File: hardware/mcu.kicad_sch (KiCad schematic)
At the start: 9 parts, among them J2 DebugEdge_02x03, SW1 RESET, U1 STM32G070CBTx_u, X1 KC2520Z

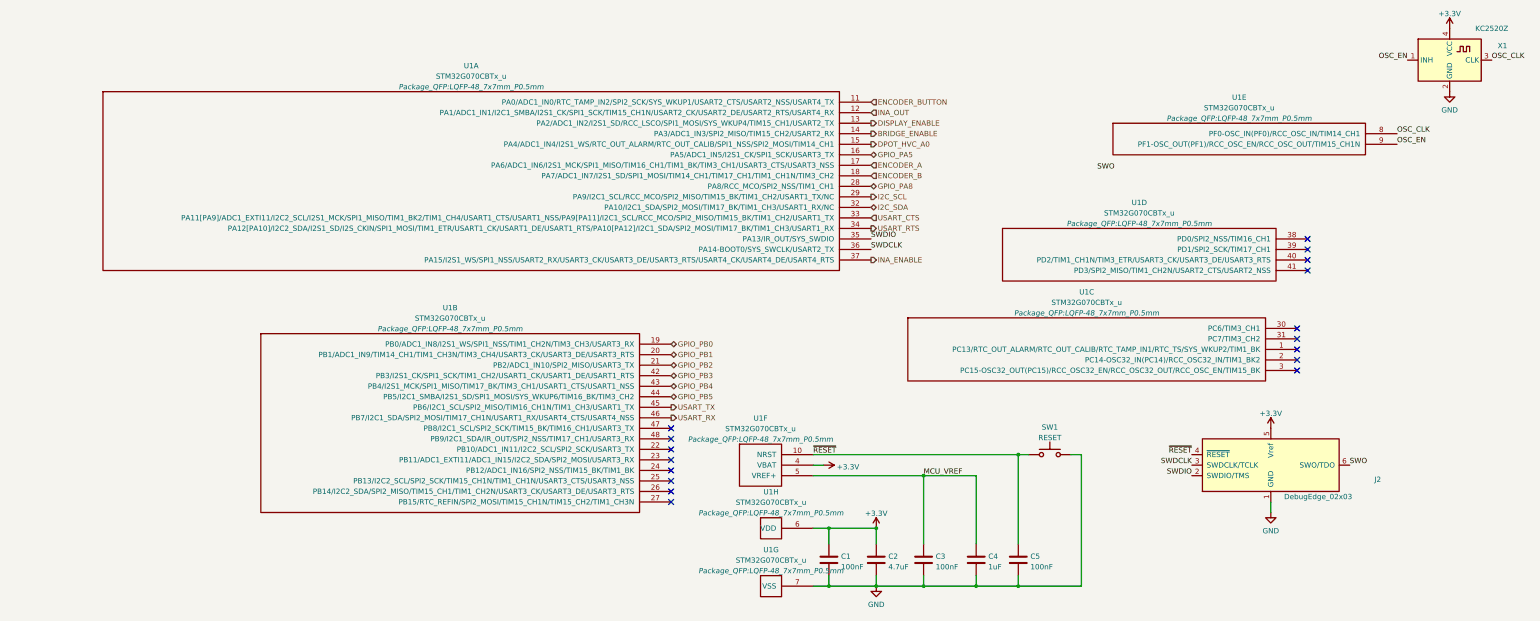
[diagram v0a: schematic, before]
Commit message: Updated schematic according to reference design
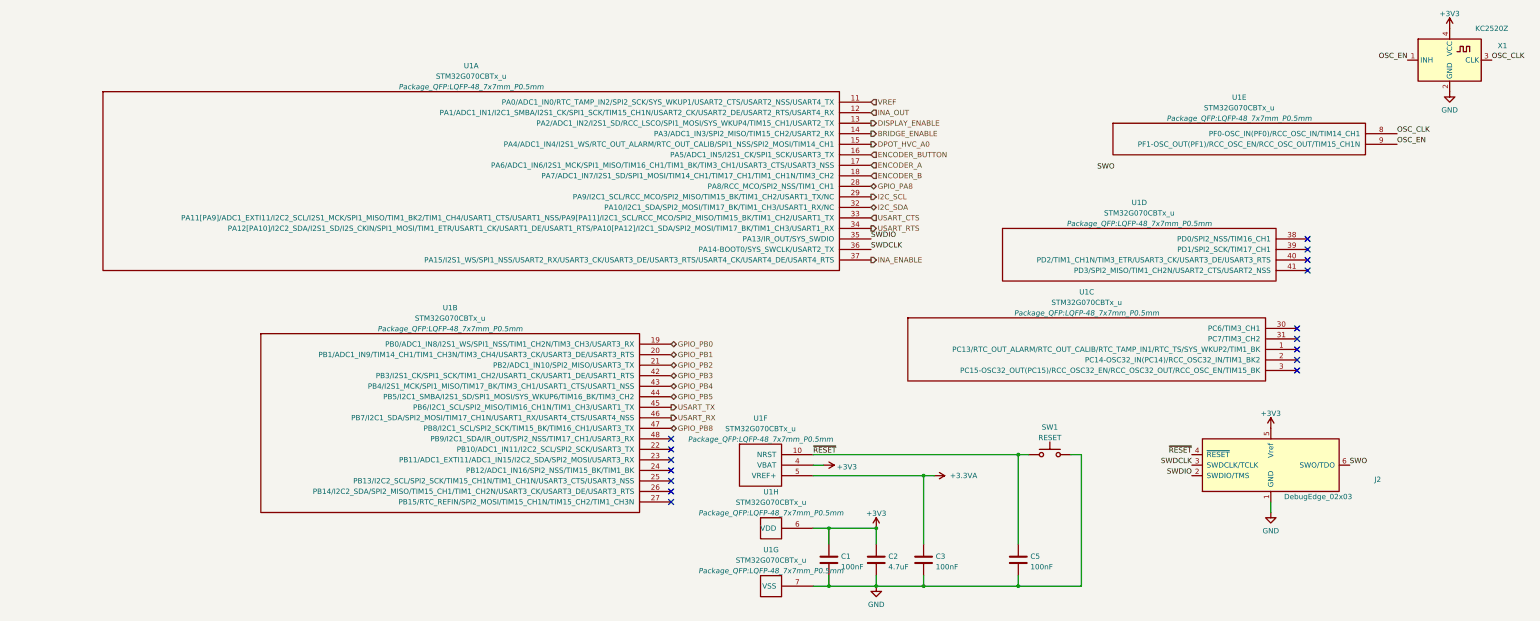
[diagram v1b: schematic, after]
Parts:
- removed C4: 1uF, Capacitor_SMD:C_0603_1608Metric_Pad1.08x0.95mm_HandSolder, symbol Device:C
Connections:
- net GPIO_PA5 is gone; now on net ENCODER_BUTTON: U1.16 (PA5/ADC1_IN5/I2S1_CK/SPI1_SCK/USART3_TX)
- net ENCODER_BUTTON: no longer U1.11 (PA0/ADC1_IN0/RTC_TAMP_IN2/SPI2_SCK/SYS_WKUP1/USART2_CTS/USART2_NSS/USART4_TX)
- net GPIO_PB8: now reaches U1.47 (PB8/I2C1_SCL/SPI2_SCK/TIM15_BK/TIM16_CH1/USART3_TX)
- net MCU_VREF renamed +3.3VA
- new net VREF: U1.11 (PA0/ADC1_IN0/RTC_TAMP_IN2/SPI2_SCK/SYS_WKUP1/USART2_CTS/USART2_NSS/USART4_TX)
- no-connect marks 17 -> 16

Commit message: Include active filter, ext. ADC, changes to power supply
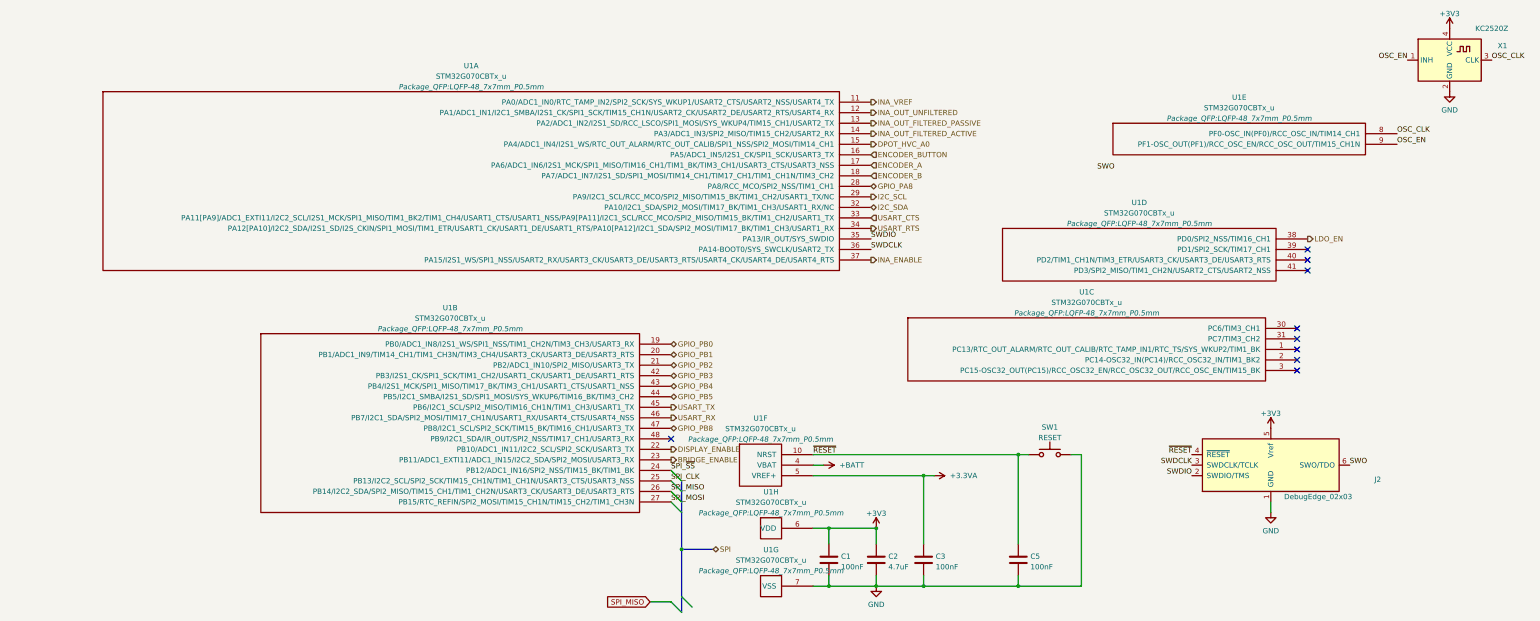
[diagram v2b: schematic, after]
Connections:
- net +3V3: no longer U1.4 (VBAT)
- net BRIDGE_ENABLE: now also U1.23 (PB11/ADC1_EXTI11/ADC1_IN15/I2C2_SDA/SPI2_MOSI/USART3_RX); no longer U1.14 (PA3/ADC1_IN3/SPI2_MISO/TIM15_CH2/USART2_RX)
- net DISPLAY_ENABLE: now also U1.22 (PB10/ADC1_IN11/I2C2_SCL/SPI2_SCK/USART3_TX); no longer U1.13 (PA2/ADC1_IN2/I2S1_SD/RCC_LSCO/SPI1_MOSI/SYS_WKUP4/TIM15_CH1/USART2_TX)
- net LDO_EN: now reaches U1.38 (PD0/SPI2_NSS/TIM16_CH1)
- net SPI_~{SS}: now reaches U1.24 (PB12/ADC1_IN16/SPI2_NSS/TIM15_BK/TIM1_BK)
- net SPI_CLK: now reaches U1.25 (PB13/I2C2_SCL/SPI2_SCK/TIM15_CH1N/TIM1_CH1N/USART3_CTS/USART3_NSS)
- net SPI_MISO: now reaches U1.26 (PB14/I2C2_SDA/SPI2_MISO/TIM15_CH1/TIM1_CH2N/USART3_CK/USART3_DE/USART3_RTS)
- net SPI_MOSI: now reaches U1.27 (PB15/RTC_REFIN/SPI2_MOSI/TIM15_CH1N/TIM15_CH2/TIM1_CH3N)
- net INA_OUT renamed INA_OUT_UNFILTERED
- net VREF renamed INA_VREF
- new net +BATT: U1.4 (VBAT)
- new net INA_OUT_FILTERED_ACTIVE: U1.14 (PA3/ADC1_IN3/SPI2_MISO/TIM15_CH2/USART2_RX)
- new net INA_OUT_FILTERED_PASSIVE: U1.13 (PA2/ADC1_IN2/I2S1_SD/RCC_LSCO/SPI1_MOSI/SYS_WKUP4/TIM15_CH1/USART2_TX)
- no-connect marks 16 -> 9

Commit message: Added correct symbol and libraries for ADC
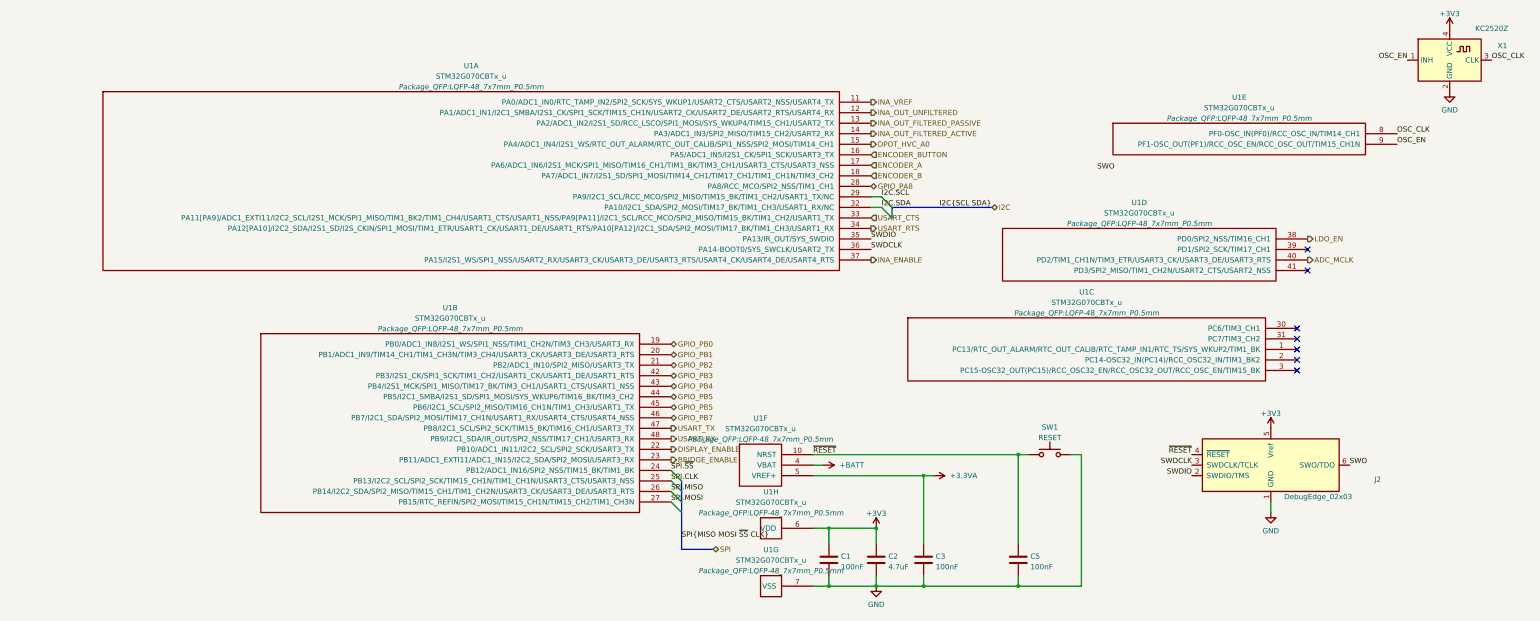
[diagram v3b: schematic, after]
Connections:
- net GPIO_PB8 is gone; now on net USART_TX: U1.47 (PB8/I2C1_SCL/SPI2_SCK/TIM15_BK/TIM16_CH1/USART3_TX)
- net GPIO_PB5: now also U1.45 (PB6/I2C1_SCL/SPI2_MISO/TIM16_CH1N/TIM1_CH3/USART1_TX)
- net USART_RX: now also U1.48 (PB9/I2C1_SDA/IR_OUT/SPI2_NSS/TIM17_CH1/USART3_RX); no longer U1.46 (PB7/I2C1_SDA/SPI2_MOSI/TIM17_CH1N/USART1_RX/USART4_CTS/USART4_NSS)
- net USART_TX: no longer U1.45 (PB6/I2C1_SCL/SPI2_MISO/TIM16_CH1N/TIM1_CH3/USART1_TX)
- net ADC_MCLK: now reaches U1.40 (PD2/TIM1_CH1N/TIM3_ETR/USART3_CK/USART3_DE/USART3_RTS)
- net I2C_SCL renamed I2C.SCL
- net I2C_SDA renamed I2C.SDA
- net SPI_CLK renamed SPI.CLK
- net SPI_MISO renamed SPI.MISO
- net SPI_MOSI renamed SPI.MOSI
- net SPI_~{SS} renamed SPI.~{SS}
- new net GPIO_PB7: U1.46 (PB7/I2C1_SDA/SPI2_MOSI/TIM17_CH1N/USART1_RX/USART4_CTS/USART4_NSS)
- no-connect marks 9 -> 7

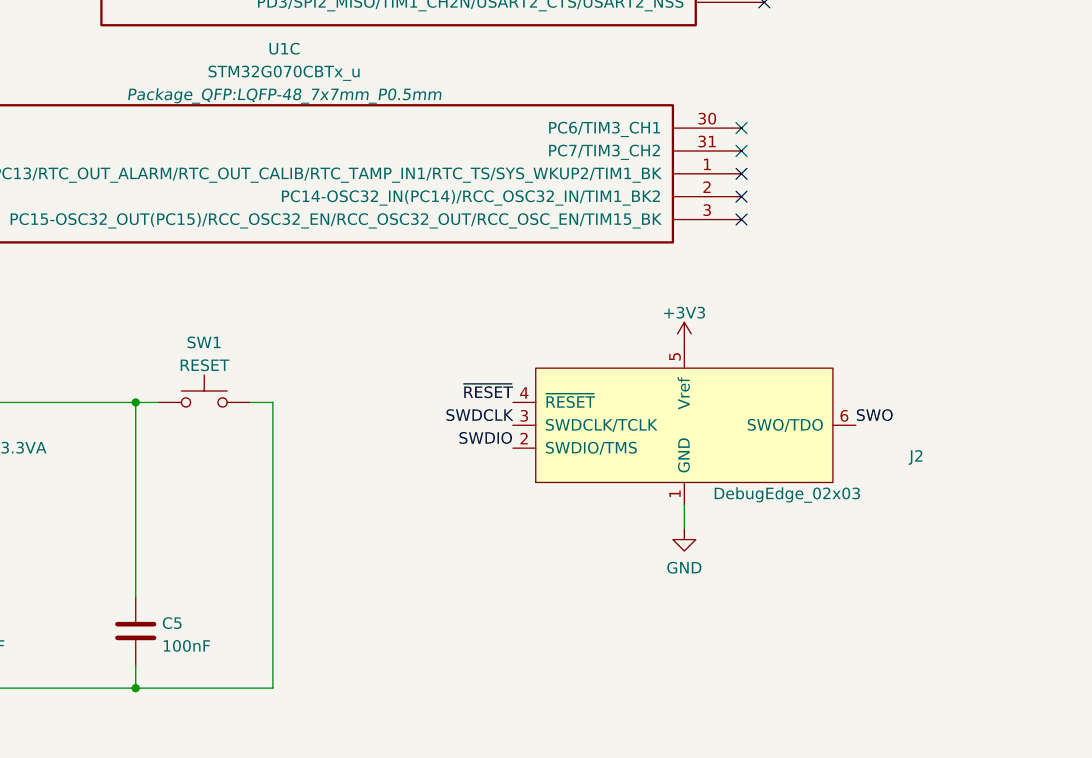
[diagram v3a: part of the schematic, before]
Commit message: Regenerated reference designators, changed to rail-to-rail op-amps
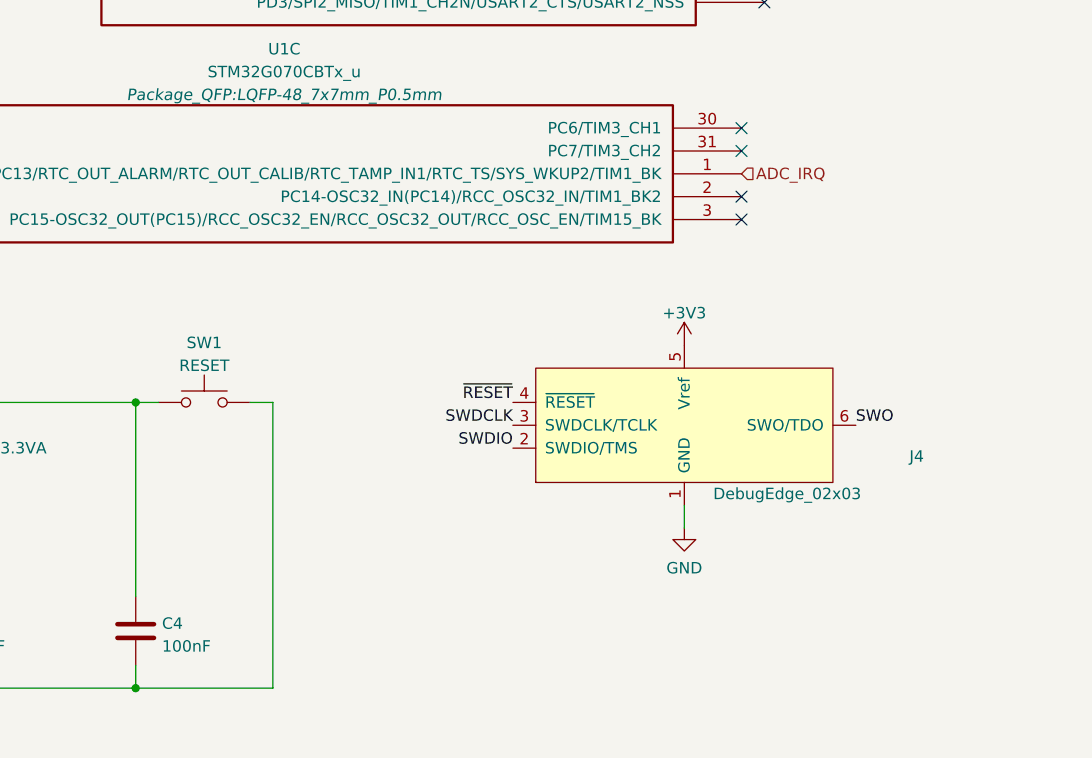
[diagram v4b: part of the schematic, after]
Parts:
- renumbered C5 to C4, J2 to J4
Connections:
- net ADC_IRQ: now reaches U1.1 (PC13/RTC_OUT_ALARM/RTC_OUT_CALIB/RTC_TAMP_IN1/RTC_TS/SYS_WKUP2/TIM1_BK)
- no-connect marks 7 -> 6
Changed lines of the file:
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@@
 	)
 	(no_connect
-		(at 229.87 119.38)
-	)
-	(no_connect
 		(at 229.87 121.92)
 	)
@@
 		)
 	)
+	(hierarchical_label "ADC_IRQ"
+		(shape input)
+		(at 229.87 119.38 0)
+		(effects
+			(font
+				(size 1.27 1.27)
+			)
+			(justify left)
+		)
+	)
 	(hierarchical_label "DISPLAY_ENABLE"
 		(shape output)
@@
 		(dnp no)
 		(fields_autoplaced yes)
-		(property "Reference" "#PWR017"
+		(property "Reference" "#PWR07"
 			(at 138.43 149.86 0)
 			(effects
@@
 			(project ""
 				(path "/adf38c8f-bada-4838-acc6-e6af19946742/e50b7c46-7cda-4158-8fd2-26ea52f7127e"
-					(reference "#PWR017")
+					(reference "#PWR07")
 					(unit 1)
 				)
@@
 		(dnp no)
 		(fields_autoplaced yes)
-		(property "Reference" "#PWR0107"
+		(property "Reference" "#PWR08"
 			(at 223.52 142.24 0)
 			(effects
@@
 			(project ""
 				(path "/adf38c8f-bada-4838-acc6-e6af19946742/e50b7c46-7cda-4158-8fd2-26ea52f7127e"
-					(reference "#PWR0107")
+					(reference "#PWR08")
 					(unit 1)
 				)
@@
 		(on_board yes)
 		(dnp no)
-		(property "Reference" "J2"
+		(property "Reference" "J4"
 			(at 249.332 150.7784 0)
 			(effects
@@
 			(project ""
 				(path "/adf38c8f-bada-4838-acc6-e6af19946742/e50b7c46-7cda-4158-8fd2-26ea52f7127e"
-					(reference "J2")
+					(reference "J4")
 					(unit 1)
 				)
@@
 		(dnp no)
 		(fields_autoplaced yes)
-		(property "Reference" "#PWR028"
+		(property "Reference" "#PWR04"
 			(at 111.76 147.32 0)
 			(effects
@@
 			(project ""
 				(path "/adf38c8f-bada-4838-acc6-e6af19946742/e50b7c46-7cda-4158-8fd2-26ea52f7127e"
-					(reference "#PWR028")
+					(reference "#PWR04")
 					(unit 1)
 				)
@@
 		(dnp no)
 		(fields_autoplaced yes)
-		(property "Reference" "#PWR0106"
+		(property "Reference" "#PWR06"
 			(at 128.27 182.88 0)
 			(effects
@@
 			(project ""
 				(path "/adf38c8f-bada-4838-acc6-e6af19946742/e50b7c46-7cda-4158-8fd2-26ea52f7127e"
-					(reference "#PWR0106")
+					(reference "#PWR06")
 					(unit 1)
 				)
@@
 		(dnp no)
 		(fields_autoplaced yes)
-		(property "Reference" "#PWR0110"
+		(property "Reference" "#PWR010"
 			(at 266.7 45.72 0)
 			(effects
@@
 			(project ""
 				(path "/adf38c8f-bada-4838-acc6-e6af19946742/e50b7c46-7cda-4158-8fd2-26ea52f7127e"
-					(reference "#PWR0110")
+					(reference "#PWR010")
 					(unit 1)
 				)
@@
 		(dnp no)
 		(fields_autoplaced yes)
-		(property "Reference" "C5"
+		(property "Reference" "C4"
 			(at 165.481 169.3453 0)
 			(effects
@@
 			(project ""
 				(path "/adf38c8f-bada-4838-acc6-e6af19946742/e50b7c46-7cda-4158-8fd2-26ea52f7127e"
-					(reference "C5")
+					(reference "C4")
 					(unit 1)
 				)
@@
 		(dnp no)
 		(fields_autoplaced yes)
-		(property "Reference" "#PWR0111"
+		(property "Reference" "#PWR011"
 			(at 266.7 63.5 0)
 			(effects
@@
 			(project ""
 				(path "/adf38c8f-bada-4838-acc6-e6af19946742/e50b7c46-7cda-4158-8fd2-26ea52f7127e"
-					(reference "#PWR0111")
+					(reference "#PWR011")
 					(unit 1)
 				)
@@
 		(dnp no)
 		(fields_autoplaced yes)
-		(property "Reference" "#PWR0104"
+		(property "Reference" "#PWR05"
 			(at 128.27 166.37 0)
 			(effects
@@
 			(project ""
 				(path "/adf38c8f-bada-4838-acc6-e6af19946742/e50b7c46-7cda-4158-8fd2-26ea52f7127e"
-					(reference "#PWR0104")
+					(reference "#PWR05")
 					(unit 1)
 				)
@@
 		(dnp no)
 		(fields_autoplaced yes)
-		(property "Reference" "#PWR0108"
+		(property "Reference" "#PWR09"
 			(at 223.52 165.1 0)
 			(effects
@@
 			(project ""
 				(path "/adf38c8f-bada-4838-acc6-e6af19946742/e50b7c46-7cda-4158-8fd2-26ea52f7127e"
-					(reference "#PWR0108")
+					(reference "#PWR09")
 					(unit 1)
 				)

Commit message: Major changes to schematic
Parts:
- C1, C2, C3, C4: footprint Capacitor_SMD:C_0603_1608Metric_Pad1.08x0.95mm_HandSolder -> Capacitor_SMD:C_0603_1608Metric
- J4: footprint custom:DebugEdge_2x03_Target -> Connector_DebugEdge:DebugEdge_2x03_Target
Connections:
- net ADC_MCLK: now also U1.39 (PD1/SPI2_SCK/TIM17_CH1); no longer U1.40 (PD2/TIM1_CH1N/TIM3_ETR/USART3_CK/USART3_DE/USART3_RTS)
- net DPOT_HVC_A0: now also U1.41 (PD3/SPI2_MISO/TIM1_CH2N/USART2_CTS/USART2_NSS); no longer U1.15 (PA4/ADC1_IN4/I2S1_WS/RTC_OUT_ALARM/RTC_OUT_CALIB/SPI1_NSS/SPI2_MOSI/TIM14_CH1)
- net LDO_EN: now also U1.3 (PC15-OSC32_OUT(PC15)/RCC_OSC32_EN/RCC_OSC32_OUT/RCC_OSC_EN/TIM15_BK); no longer U1.38 (PD0/SPI2_NSS/TIM16_CH1)
- net I2C.SCL renamed I2C1.SCL
- net I2C.SDA renamed I2C1.SDA
- net SPI.CLK renamed SPI2.CLK
- net SPI.MISO renamed SPI2.MISO
- net SPI.MOSI renamed SPI2.MOSI
- net SPI.~{SS} renamed SPI2.~{SS}
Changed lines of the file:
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@@
 	)
 	(no_connect
-		(at 232.41 100.33)
+		(at 127 69.85)
 	)
 	(no_connect
-		(at 232.41 95.25)
+		(at 232.41 97.79)
 	)
 	(no_connect
@@
 	)
 	(no_connect
-		(at 229.87 124.46)
+		(at 232.41 92.71)
 	)
 	(no_connect
@@
 	(bus
 		(pts
-			(xy 81.28 167.64) (xy 88.9 167.64)
+			(xy 81.28 167.64) (xy 83.82 167.64)
 		)
 		(stroke
@@
 			(width 0)
 			(type default)
-		)
-	)
-	(label "SPI{MISO MOSI ~{SS} CLK}"
-		(at 81.28 165.1 0)
-		(effects
-			(font
-				(size 1.27 1.27)
-			)
-			(justify left bottom)
 		)
 	)
@@
 		)
 	)
-	(label "SPI.MOSI"
+	(label "SPI2.MOSI"
 		(at 78.74 156.21 0)
 		(effects
@@
 		)
 	)
-	(label "SPI.CLK"
+	(label "SPI2.CLK"
 		(at 78.74 151.13 0)
 		(effects
@@
 		)
 	)
-	(label "SPI.~{SS}"
+	(label "SPI2.~{SS}"
 		(at 78.74 148.59 0)
 		(effects
@@
 		)
 	)
-	(label "I2C{SCL SDA}"
-		(at 143.51 85.09 0)
-		(effects
-			(font
-				(size 1.27 1.27)
-			)
-			(justify left bottom)
-		)
-	)
 	(label "SWDCLK"
 		(at 204.47 147.32 180)
@@
 		)
 	)
-	(label "I2C.SDA"
+	(label "I2C1.SDA"
 		(at 129.54 85.09 0)
 		(effects
@@
 		)
 	)
-	(label "I2C.SCL"
+	(label "I2C1.SCL"
 		(at 129.54 82.55 0)
 		(effects
@@
 		)
 	)
-	(label "SPI.MISO"
+	(label "SPI2.MISO"
 		(at 78.74 153.67 0)
 		(effects
@@
 		)
 	)
-	(hierarchical_label "SPI"
+	(hierarchical_label "SPI2{SPI}"
 		(shape bidirectional)
-		(at 88.9 167.64 0)
-		(effects
-			(font
-				(size 1.27 1.27)
-			)
-			(justify left)
-		)
-	)
-	(hierarchical_label "I2C"
+		(at 83.82 167.64 0)
+		(effects
+			(font
+				(size 1.27 1.27)
+			)
+			(justify left)
+		)
+	)
+	(hierarchical_label "I2C1{I2C}"
 		(shape bidirectional)
 		(at 156.21 85.09 0)
@@
 	(hierarchical_label "LDO_EN"
 		(shape output)
-		(at 232.41 92.71 0)
+		(at 229.87 124.46 0)
 		(effects
 			(font
@@
 	(hierarchical_label "DPOT_HVC_A0"
 		(shape output)
-		(at 127 69.85 0)
+		(at 232.41 100.33 0)
 		(effects
 			(font
@@
 	(hierarchical_label "ADC_MCLK"
 		(shape output)
-		(at 232.41 97.79 0)
+		(at 232.41 95.25 0)
 		(effects
 			(font
@@
 			)
 		)
-		(property "Footprint" "custom:DebugEdge_2x03_Target"
+		(property "Footprint" "Connector_DebugEdge:DebugEdge_2x03_Target"
 			(at 223.52 157.48 0)
 			(effects
@@
 			)
 		)
-		(property "Footprint" "Capacitor_SMD:C_0603_1608Metric_Pad1.08x0.95mm_HandSolder"
+		(property "Footprint" "Capacitor_SMD:C_0603_1608Metric"
 			(at 129.2352 173.99 0)
 			(effects
@@
 			)
 		)
-		(property "Footprint" "Capacitor_SMD:C_0603_1608Metric_Pad1.08x0.95mm_HandSolder"
+		(property "Footprint" "Capacitor_SMD:C_0603_1608Metric"
 			(at 140.6652 173.99 0)
 			(effects
@@
 			)
 		)
-		(property "Footprint" "Capacitor_SMD:C_0603_1608Metric_Pad1.08x0.95mm_HandSolder"
+		(property "Footprint" "Capacitor_SMD:C_0603_1608Metric"
 			(at 163.5252 173.99 0)
 			(effects
@@
 			)
 		)
-		(property "Footprint" "Capacitor_SMD:C_0603_1608Metric_Pad1.08x0.95mm_HandSolder"
+		(property "Footprint" "Capacitor_SMD:C_0603_1608Metric"
 			(at 117.8052 173.99 0)
 			(effects
